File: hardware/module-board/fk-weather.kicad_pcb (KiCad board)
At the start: 2 copper layers, 37.5 x 103 mm, 74 parts, among them J1 MICRO-USB, J10 CONN_01x06, J11 CONN_01x06, J2 CONN_01x05, J3 CONN_01x03_SERIAL, J4 CONN_01x04, J5 CONN_01x02, J6 CONN_02x05_SWD, J7 CONN_01x05, M1 MOUNT_HOLE, M2 MOUNT_HOLE, M3 MOUNT_HOLE, M4 MOUNT_HOLE, Q4 2N7002LT1G, SW1 SPNO, U1 ATSAMD21G18A-AU, U2 MCP1700T-3302E/MB, U3 TPS2051B, U4 S25FL116K0XMFI041, U5 SK6812, U6 PCF8523, Y1 FC-135, Y2 FC-135

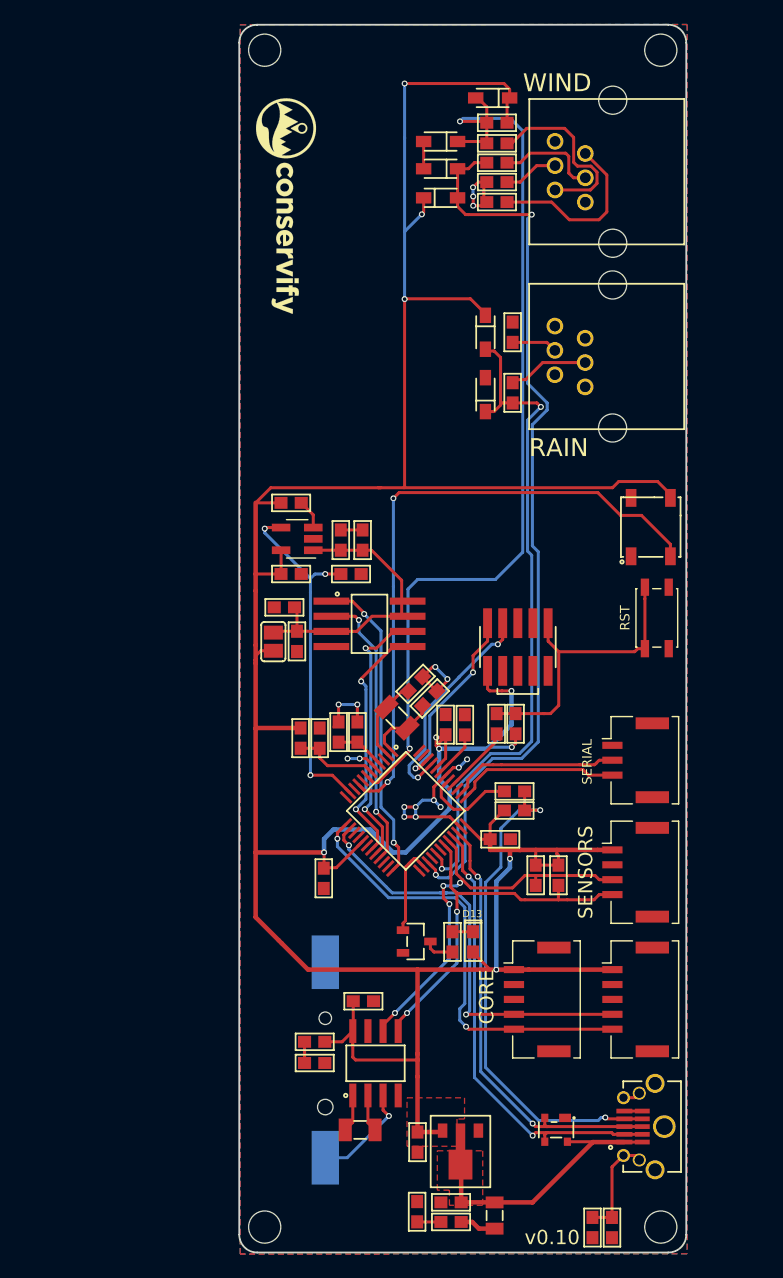
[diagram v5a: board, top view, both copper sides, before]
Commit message: Started replacing parts on the weather board, including the USB connectors and the switching component
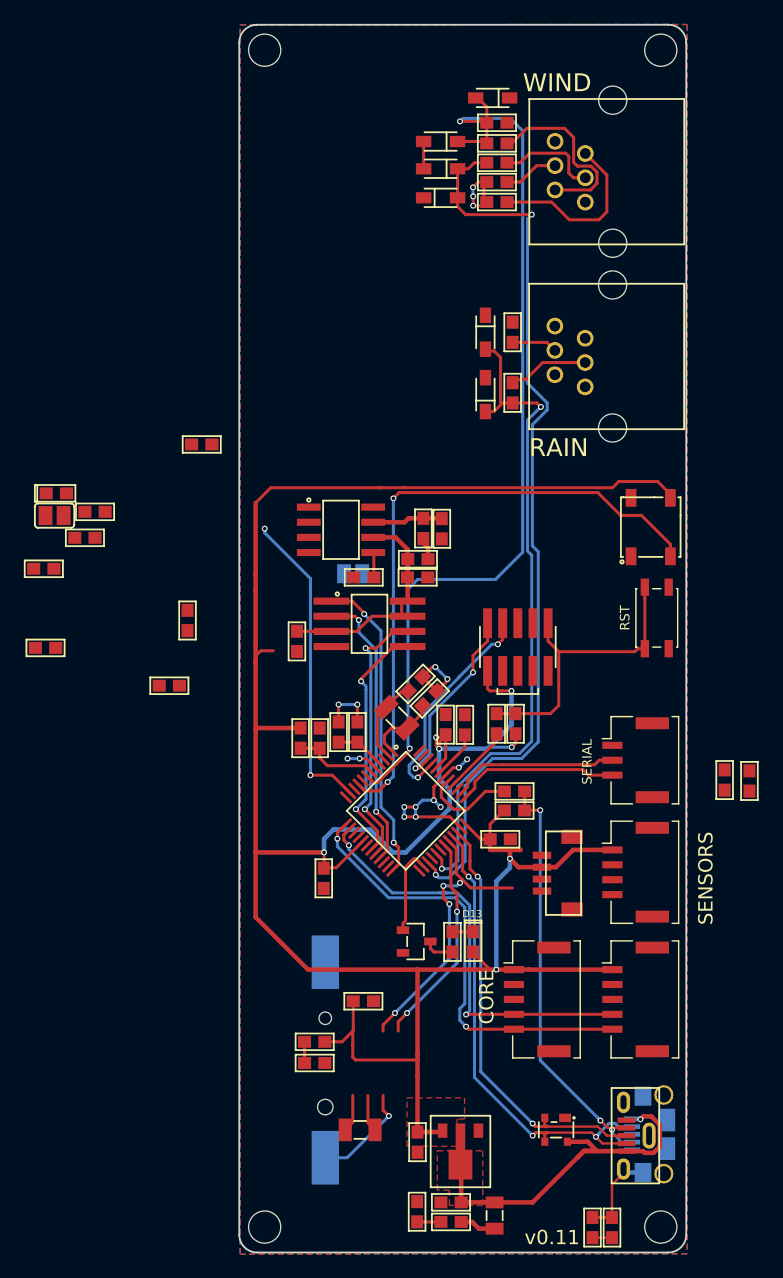
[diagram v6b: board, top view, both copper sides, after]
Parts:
- removed G***: LOGO, conservify:conservify_text_negative_4000
- removed U6: PCF8523, conservify:SOIC-8-N
- added C20: 100nF, conservify:CAP-0603, F.Cu at (99.6, 142.1)
- added C21: 10uF, conservify:CAP-0603, F.Cu at (99.6, 143.7)
- added D1: Green, conservify:LED-0603, F.Cu at (69.3, 136.6)
- added J12: CONN_01x02, conservify:SJ_OPEN, B.Cu at (94.2, 143.4)
- added J8: CONN_01x04, conservify:BM04B-SRSS-TB, F.Cu at (111.3, 168.5)
- added J9: CONN_01x02, conservify:SJ_OPEN, F.Cu at (69.1, 138.5)
- added R12: 10K, conservify:RES-0603, F.Cu at (95.0, 143.7)
- added R13: ?, conservify:RES-0603, F.Cu at (72.5, 138.2)
- added R14: 100K, conservify:RES-0603, F.Cu at (71.7, 140.3)
- added R15: 100K, conservify:RES-0603, F.Cu at (68.2, 142.9)
- C15: value 100nF -> 10uF
- C16: value 10uF -> 100nF
- J1: footprint conservify:MICRO-USB -> conservify:USB_1051330011
- J5: value CONN_01x02 -> MICRO-USB; footprint conservify:SJ_OPEN -> conservify:USB_10118193-0001LF-core-mod; moved to B.Cu
- R11: value 10K -> ?
- R3: value ? -> 2k2
- R5: value ? -> 10K
- U3: value TPS2051B -> TPS2052B; footprint conservify:SOT-23-5_HandSoldering -> conservify:SOIC-8-N
- moved J5 53.6 mm to (121.7, 190.4), turned to 270 degrees
- moved R3 26.4 mm to (68.4, 149.6)
- moved R6 17.9 mm to (127.4, 160.7)
- moved R7 17.7 mm to (125.3, 160.7)
- moved C16 14.5 mm to (80.3, 147.3)
- moved C13 11.7 mm to (100.1, 139.6), turned to 270 degrees
- moved R5 11.7 mm to (78.7, 152.8)
- moved R11 8.96 mm to (81.5, 132.5)
- moved C15 6.72 mm to (101.6, 139.6), turned to 270 degrees
- moved U3 3.75 mm to (93.1, 139.7), turned to 0 degrees
- moved J1 1.70 mm to (116.8, 190.5)
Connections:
- C11 pad 1: VUSB -> 5V0
- C13 pad 1: 3V3 -> /WEATHER_3V3
- C15 pad 1: /PERIPH_3V3 -> /WEATHER_3V3
- C16 pad 1: /PERIPH_3V3 -> 3V3
- D10 pad 1: 3V3 -> /WEATHER_3V3
- D6 pad 1: 3V3 -> /WEATHER_3V3
- D9 pad 1: 3V3 -> /WEATHER_3V3
- J5 pad 1: 3V3 -> VUSB
- J5 pad 2: /PERIPH_3V3 -> /USB-
- R11 pad 1: Net-(R11-Pad1) -> /D7_WEATHER_EN
- R11 pad 2: 3V3 -> GND
- R3 pad 1: GND -> Net-(D1-Pad1)
- R3 pad 2: /D8_PERIPH_EN -> GND
- R34 pad 1: 3V3 -> /WEATHER_3V3
- R5 pad 1: GND -> Net-(R5-Pad1)
- R5 pad 2: /PERIPH_3V3 -> 3V3
- U1 pad 30: /D7 -> /D7_WEATHER_EN
- U2 pad 2: VUSB -> 5V0
- U3 pad 1: /PERIPH_3V3 -> GND
- U3 pad 2: GND -> 3V3
- U3 pad 3: Net-(R11-Pad1) -> /D7_WEATHER_EN
- U3 pad 4: /D8_PERIPH_EN -> /D12_PERIPH_EN
- U3 pad 5: 3V3 -> Net-(R12-Pad1)
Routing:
- net 3V3: track 291.5 -> 225.7 mm, vias 10 -> 7
- net /SDA1: track 33.3 -> 18.7 mm
- net /SCL1: track 34.8 -> 24.7 mm
- net VUSB: track 25.4 -> 33.4 mm, vias 0 -> 1
- net /PERIPH_3V3: track 26.2 -> 19.7 mm
- net /WEATHER_3V3: track 0.00 -> 6.08 mm
- net Net-(J1-Pad4): track 42.6 -> 37.1 mm, vias 2 -> 3
- net /D8_PERIPH_EN: track 30.4 -> 26.4 mm, vias 3 -> 2
- net /USB-: track 38.1 -> 40.8 mm, vias 2 -> 3
- net Net-(R11-Pad1): track 2.49 -> 0.00 mm
- net Net-(R12-Pad1): track 0.00 -> 2.11 mm
- net Net-(J1-Pad7): track 1.48 -> 0.00 mm
- net /USB+: track 37.2 -> 36.2 mm
- net Net-(C10-Pad1): track 8.72 -> 7.85 mm
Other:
- board text added: "v0.11"
- board text removed: "v0.10"

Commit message: Swapped to 4 layer
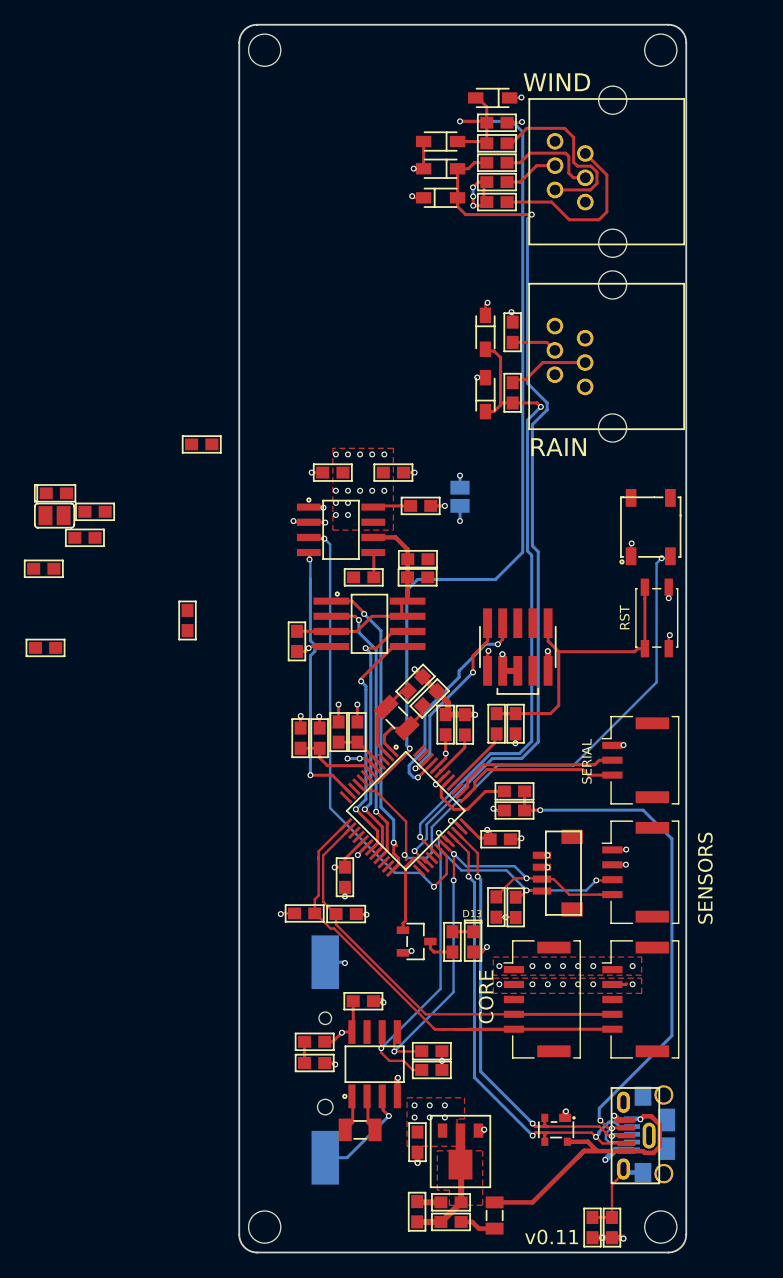
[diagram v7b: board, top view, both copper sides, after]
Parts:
- added R16: 4.7K, conservify:RES-0603, F.Cu at (90.1, 171.9)
- added R18: 4.7K, conservify:RES-0603, F.Cu at (93.6, 171.9)
- added R19: 4.7K, conservify:RES-0603, F.Cu at (100.8, 183.4)
- added R20: 4.7K, conservify:RES-0603, F.Cu at (100.8, 185.0)
- added U6: PCF8523, conservify:SOIC-8-N, F.Cu at (96.0, 184.5)
- moved R5 25.9 mm to (99.8, 137.7)
- moved R6 23.7 mm to (106.2, 171.3), turned to 270 degrees
- moved R7 20.5 mm to (107.8, 171.3), turned to 270 degrees
- moved J12 11.0 mm to (103.1, 136.9), turned to 90 degrees
- moved C13 8.92 mm to (92.5, 134.9), turned to 180 degrees
- moved C15 6.22 mm to (97.5, 134.9), turned to 0 degrees
- moved C8 1.78 mm to (93.5, 168.8)
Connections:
- R13 pad 1: /D12_PERIPH_EN -> /D8_PERIPH_EN
- U3 pad 4: /D12_PERIPH_EN -> /D8_PERIPH_EN
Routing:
- net 3V3: track 225.7 -> 33.4 mm, vias 7 -> 32
- net /D7_WEATHER_EN: track 0.00 -> 39.4 mm, vias 0 -> 2
- net GND: track 41.4 -> 64.8 mm, vias 17 -> 49
- net /SDA1: track 18.7 -> 41.7 mm, vias 2 -> 4
- net /SCL1: track 24.7 -> 45.7 mm
- net /SDA2: track 37.7 -> 49.4 mm, vias 2 -> 0
- net Net-(J1-Pad4): track 37.1 -> 48.4 mm
- net VUSB: track 33.4 -> 25.1 mm
- net 5V0: track 2.02 -> 9.84 mm
- net /A3: track 53.2 -> 48.9 mm
- net /D8_PERIPH_EN: track 26.4 -> 23.0 mm
- net Net-(R5-Pad1): track 0.00 -> 3.17 mm
- net /D10_WIND_SPEED: track 76.6 -> 74.5 mm
- net /D6_RAIN: track 56.5 -> 54.7 mm
- net /USB+: track 36.2 -> 38.0 mm, vias 2 -> 3
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- added copper zone on F.Cu, net /WEATHER_3V3
- added copper zone on PWR, net /WEATHER_3V3
- added copper zone on PWR, net 3V3
- added copper zone on GND, net GND
- removed copper zone on B.Cu, net GND
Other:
- copper layers 2 -> 4

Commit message: Finished v0.11, generated gerbers
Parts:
- added G***: LOGO, conservify:LOGO_CONSERVIFY_TEXT_NEGATIVE_4000, F.Cu at (94.8, 117.8)
- added G***: LOGO, conservify:LOGO_FK_NEGATIVE_2500, F.Cu at (99.8, 120.3)
- added G***: LOGO, conservify:LOGO_OSH_NEGATIVE_3000, F.Cu at (90.6, 197.8)
- J9: moved to B.Cu
- moved D1 63.3 mm to (108.9, 186.0), turned to 180 degrees
- moved R3 57.3 mm to (112.6, 186.1), turned to 0 degrees
- moved J9 31.4 mm to (99.6, 146.0), turned to 180 degrees
- moved R14 29.8 mm to (101.4, 140.4)
- moved R15 28.6 mm to (94.8, 132.5), turned to 90 degrees
- moved R13 15.4 mm to (87.3, 142.3), turned to 180 degrees
- moved C16 11.6 mm to (87.7, 138.4)
- moved R11 10.2 mm to (87.3, 140.8)
- moved Y1 1.32 mm to (97.0, 154.4)
- moved C2 0.88 mm to (100.3, 153.0)
- moved R8 0.88 mm to (108.1, 162.5)
- moved R9 0.85 mm to (108.1, 160.9)
- moved C1 0.79 mm to (99.1, 151.9)
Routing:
- net GND: track 64.8 -> 76.6 mm, vias 49 -> 56
- net /PERIPH_3V3: track 19.7 -> 27.5 mm, vias 0 -> 1
- net 3V3: track 33.4 -> 38.9 mm, vias 32 -> 36
- net /A1_WIND_DIR: track 79.5 -> 75.4 mm
- net /D8_PERIPH_EN: track 23.0 -> 25.6 mm
- net /D7_WEATHER_EN: track 39.4 -> 41.9 mm
- net Net-(D1-Pad1): track 0.00 -> 2.00 mm
- net Net-(C1-Pad2): track 7.12 -> 8.27 mm
- net /USB_ID: track 8.00 -> 8.73 mm
- net /WEATHER_3V3: vias 19 -> 18
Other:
- board text added: "PWR"
- board text added: "Weather v0.11"
- board text removed: "v0.11"
